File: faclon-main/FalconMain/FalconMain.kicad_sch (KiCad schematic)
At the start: 193 parts, among them J1 Nano-Fit, J2 PTH, J3 Nano-Fit, J4 100mil, J5 Nano-Fit, J6 100mil, J7 Nano-Fit, J8 DNP, J9 JST-XH, Q1 Q_PMOS_GDS, Q10 Q_NMOS_GSD, Q11 Q_PMOS_GSD, Q12 Q_PMOS_GSD, Q13 Q_PMOS_GSD, Q14 Q_PMOS_GSD, Q15 Q_NMOS_GSD, Q16 Q_PMOS_GSD, Q17 Q_PMOS_GSD, Q18 Q_PMOS_GSD, Q19 Q_PMOS_GSD, Q2 Q_PMOS_GDS, Q20 Q_NMOS_GSD, Q21 Q_NMOS_GSD, Q22 Q_PMOS_GDS, Q23 Q_NMOS_GSD, Q24 Q_PMOS_GSD, Q3 Q_NMOS_GDS, Q4 Q_NMOS_GDS, Q5 Q_PMOS_GDS, Q6 Q_PMOS_GDS, Q7 Q_NMOS_GSD, Q8 Q_NMOS_GSD, Q9 Q_NMOS_GSD, U1 MAX1873TEEE+, U2 ADP1883ARMZ-0.6-R7, U3 LTC4412ES6#TRPBF, U4 STM32L152CBT6, U5 BD9E104FJ-E2, U6 AL8843QSP-13, U7 NCP164ASN330T1G, Y1 8MHz, Y2 32.768kHz

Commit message: Design freeze maybe
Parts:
- removed C24, C?: 100uF, Capacitor_THT:CP_Radial_D8.0mm_P3.50mm, symbol Device:C_Polarized_Small
- removed D1, D3, D?: DNP, symbol Device:D_Schottky_Small
- removed Q1, Q5, Q6: Q_PMOS_GDS, symbol Device:Q_PMOS_GDS
- removed R1: 1M, Resistor_SMD:R_0402_1005Metric, symbol Device:R_Small
- removed R18: 0R, Resistor_SMD:R_0402_1005Metric, symbol Device:R_Small
- removed R2: 100k, Resistor_SMD:R_0402_1005Metric, symbol Device:R_Small
- removed R21: 442k, Resistor_SMD:R_0402_1005Metric, symbol Device:R_Small
- removed U3: LTC4412ES6#TRPBF, symbol JetkovKiCADLib:LTC4412ES6#TRPBF
- added C?: 100uF, Capacitor_THT:CP_Radial_D8.0mm_P3.50mm, symbol Device:C_Polarized_Small
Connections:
- net VDC_METERED is gone; now on net VSYS: Q2.3 (S), R13.2, R14.1
- net GND: now also C?.2
- net VSYS: now also C?.1
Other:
- note added: "Charger enabled if DCIN>BATT+220mV Charger disabled if DCIN<BATT+50mV"
- note added: "Design such that diode can replace FET"
- note added: "EXT drives to DCIN-5V"
- note added: "H: VSYS L: VSYS-4.42V"
- note added: "STAT low when SENSE>VIN+20mV Vf of FET Diode < 19.5-17-0.02=2.48V"
- note added: "VDC=VBAT if charger is discconected"
- note added: "Vf(diode)=0.8V"
- note removed: "Can we just use the one ideal diode controller here?"
- note removed: "High: VSYS Low: VSYS-4.42V"
- note removed: "charger"
- moved on the sheet: C1, Q?, R?, U?

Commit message: Finishing up schematics - part footprints
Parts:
- removed Q3, Q4: Q_NMOS_GDS, symbol Device:Q_NMOS_GDS
- added Q2, Q3: Q_NMOS_LFPAK, JetkovKiCADLib:LFPACK56-S08_SOT669_NXP, symbol JetkovKiCADLib:Q_NMOS_LFPAK
- J1, J7: footprint (none) -> JetkovKiCADLib:Molex_Nano-Fit_105309-xx05_1x05_P2.50mm_Vertical
- J2: footprint (none) -> JetkovKiCADLib:Conn_Batt_Wire_10AWG
- J3: footprint (none) -> JetkovKiCADLib:Molex_Nano-Fit_105310-xx12_2x06_P2.50mm_Vertical
- J4: footprint (none) -> Connector_PinHeader_2.54mm:PinHeader_2x03_P2.54mm_Vertical
- J5: footprint (none) -> JetkovKiCADLib:Molex_Nano-Fit_105309-xx02_1x02_P2.50mm_Vertical
- J6: footprint (none) -> Connector_PinHeader_2.54mm:PinHeader_2x15_P2.54mm_Vertical
- J8: footprint (none) -> Connector_PinHeader_2.54mm:PinHeader_1x03_P2.54mm_Vertical
- J9: footprint (none) -> Connector_JST:JST_XH_B5B-XH-AM_1x05_P2.50mm_Vertical
- U2: footprint (none) -> JetkovKiCADLib:10-MSOP_RM-10_AD
- Y1: footprint (none) -> JetkovKiCADLib:Crystal_SMD_HC49_WURTH
- Y2: footprint (none) -> Crystal:Crystal_DS26_D2.0mm_L6.0mm_Horizontal
- gave numbers to parts that had none: 6
- renumbered C20 to C21, C21 to C22, C22 to C23, C23 to C24, D2 to D1, D4 to D2, D5 to D3, D6 to D4, Q2 to Q1, Q11 to Q10, Q12 to Q11, Q13 to Q12, Q14 to Q13, Q15 to Q14, Q16 to Q15, Q17 to Q16, Q18 to Q17, Q19 to Q18, Q20 to Q19, Q21 to Q20, Q22 to Q21, Q23 to Q22, Q24 to Q23, Q7 to Q6, Q8 to Q7, Q9 to Q8, Q10 to Q9, R3 to R1, R12 to R10, R13 to R11, R14 to R12, R15 to R13, R16 to R14, R17 to R15, R19 to R17, R20 to R18, R4 to R2, R22 to R20, R23 to R21, R24 to R22, R25 to R23, R26 to R24, R27 to R25, R28 to R26, R29 to R27, R30 to R28, R31 to R29, R5 to R3, R32 to R30, R33 to R31, R34 to R32, R35 to R33, R36 to R34, R37 to R35, R38 to R36, R39 to R37, R40 to R38, R41 to R39, R6 to R4, R42 to R40, R43 to R41, R44 to R42, R45 to R43, R46 to R44, R47 to R45, R48 to R46, R49 to R47, R50 to R48, R51 to R49, R7 to R5, R52 to R50, R53 to R51, R54 to R52, R55 to R53, R56 to R54, R57 to R55, R58 to R56, R59 to R57, R60 to R58, R61 to R59, R8 to R6, R62 to R60, R63 to R61, R64 to R62, R65 to R63, R66 to R64, R67 to R65, R68 to R66, R69 to R67, R9 to R7, R10 to R8, R11 to R9
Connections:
- net GND: now also Q3.1 (S), Q3.2 (S), Q3.3 (S)
- net VSYS_SW: now also Q2.5 (D)
- net at R15.1: now also Q2.4 (G)
- net at C19.2, L2.1, R18.2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: now also Q2.1 (S), Q2.2 (S), Q2.3 (S), Q3.5 (D)
- net at R17.2, U2.6 (DRVL): now also Q3.4 (G)

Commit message: Add some footprints
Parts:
- removed Q1, Q21, Q4, Q5: Q_PMOS_GDS, symbol Device:Q_PMOS_GDS
- added Q1, Q21, Q4, Q5: Q_PMOS_LFPAK, JetkovKiCADLib:LFPACK56-S08_SOT669_NXP, symbol JetkovKiCADLib:Q_PMOS_LFPAK
- C17, C19, C24, C25, C29, C34, C36, C43, C46, C47, C5: Manufacturer Würth Elektronik -> Murata Electronics; Part Number 885012205061 -> GRM155R71E104KE14D; Voltage 50V -> 25V
- D1, D4: value D_Schottky_Small -> 20A; footprint (none) -> JetkovKiCADLib:TO-252-2-3_DPAK_ST
- D2, D3: footprint (none) -> JetkovKiCADLib:SC-76-SOD-323_USC_TSB
- L1: footprint (none) -> JetkovKiCADLib:DR125-220-R_Handsolder
- L2: footprint (none) -> JetkovKiCADLib:WE-HCI_1365_7443551
- L5: footprint (none) -> JetkovKiCADLib:AMDLA1306S
- Q10, Q11, Q12, Q13, Q15, Q16, Q17, Q18, Q23: footprint (none) -> JetkovKiCADLib:SC-96_TSMT3_ROM
- Q14, Q19, Q20, Q22, Q6, Q7, Q8, Q9: footprint (none) -> JetkovKiCADLib:SOT-323_SC-70
- R14: footprint Resistor_SMD:R_1206_3216Metric -> Resistor_SMD:R_0612_1632Metric; Manufacturer Susumu -> Rohm Semiconductor; Part Number KRL1632E-M-R068-F-T5 -> LTR18EZPFSR068; Power 0.75W -> 1W
- R46, R5: Manufacturer Stackpole Electronics Inc -> Bourns Inc.; Part Number RMCF0402FT133K -> CR0402-FX-1333GLF
- U3: footprint (none) -> JetkovKiCADLib:SOT-23-6_TSOT-23-6_LT
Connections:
- net +19V5: now also Q5.5 (D)
- net VBAT: now also Q4.5 (D)
- net VDC: now also Q4.1 (S), Q4.2 (S), Q4.3 (S), Q5.1 (S), Q5.2 (S), Q5.3 (S)
- net VSYS: now also Q1.1 (S), Q1.2 (S), Q1.3 (S), Q21.1 (S), Q21.2 (S), Q21.3 (S)
- net VSYS_SW: now also Q21.5 (D)
- net at R19.1, U3.4 (STAT): now also Q5.4 (G)
- net at C55.2, Q23.1 (G), R65.2: now also Q21.4 (G)
- net at U1.14 (EXT): now also Q1.4 (G)
- net at D1.1 (K), L1.1: now also Q1.5 (D)
- net at U3.5 (GATE): now also Q4.4 (G)
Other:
- note added: "Could place zener across capacitor to ensure fixed clamp voltage"

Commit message: Reorganize
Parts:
- removed C1, C2: 220nF, Capacitor_SMD:C_0603_1608Metric, symbol Device:C_Small
- removed C10, C16, C18, C22, C3, C45, C50, C51, C52: 10uF, Capacitor_SMD:C_1210_3225Metric, symbol Device:C_Small
- removed C11, C12, C55: 10nF, Capacitor_SMD:C_0402_1005Metric, symbol Device:C_Small
- removed C13, C14: 47nF, Capacitor_SMD:C_0402_1005Metric, symbol Device:C_Small
- removed C15: 1nF, Capacitor_SMD:C_0402_1005Metric, symbol Device:C_Small
- removed C17, C19, C46, C47, C5: 100nF, Capacitor_SMD:C_0402_1005Metric, symbol Device:C_Small
- removed C20, C8: 100uF, Capacitor_THT:CP_Radial_D8.0mm_P3.50mm, symbol Device:C_Polarized_Small
- removed C21: 33uF, Capacitor_THT:CP_Radial_D6.3mm_P2.50mm, symbol Device:C_Polarized_Small
- removed C23: 1.5nF, Capacitor_SMD:C_0402_1005Metric, symbol Device:C_Small
- removed C26, C28, C30, C33: 47uF, Capacitor_SMD:C_1210_3225Metric, symbol Device:C_Small
- removed C35: DNP, Capacitor_THT:CP_Radial_D8.0mm_P3.50mm, symbol Device:C_Polarized_Small
- removed C39, C4, C40, C41, C42, C53, C54, C6: 1uF, Capacitor_SMD:C_0603_1608Metric, symbol Device:C_Small
- removed C48, C9: 510pF, Capacitor_SMD:C_0402_1005Metric, symbol Device:C_Small
- removed C49: 12pF, Capacitor_SMD:C_0402_1005Metric, symbol Device:C_Small
- removed C7: 51pF, Capacitor_SMD:C_0402_1005Metric, symbol Device:C_Small
- removed D1, D4: 20A, JetkovKiCADLib:TO-252-2-3_DPAK_ST, symbol Device:D_Schottky_Small
- removed D2, D3: 500mA, JetkovKiCADLib:SC-76-SOD-323_USC_TSB, symbol Device:D_Schottky_Small
- removed L1: 22uH, JetkovKiCADLib:DR125-220-R_Handsolder, symbol Device:L_Small
- removed L2: 2.0uH, JetkovKiCADLib:WE-HCI_1365_7443551, symbol Device:L_Small
- removed L4: 10uH, Inductor_SMD:L_1008_2520Metric, symbol Device:L_Small
- removed L5: 47uH, JetkovKiCADLib:AMDLA1306S, symbol Device:L_Small
- removed Q1, Q21, Q4, Q5: Q_PMOS_LFPAK, JetkovKiCADLib:LFPACK56-S08_SOT669_NXP, symbol JetkovKiCADLib:Q_PMOS_LFPAK
- removed Q10, Q11, Q12, Q13, Q15, Q16, Q17, Q18, Q23: Q_PMOS_GSD, JetkovKiCADLib:SC-96_TSMT3_ROM, symbol Device:Q_PMOS_GSD
- removed Q14, Q19, Q20, Q22, Q6, Q7, Q8, Q9: Q_NMOS_GSD, JetkovKiCADLib:SOT-323_SC-70, symbol Device:Q_NMOS_GSD
- removed Q2, Q3: Q_NMOS_LFPAK, JetkovKiCADLib:LFPACK56-S08_SOT669_NXP, symbol JetkovKiCADLib:Q_NMOS_LFPAK
- removed R1, R17, R22, R23, R24, R25, R26, R27, R28, R29, R34, R35, R54, R55, R56, R61, R65, R66: 100k, Resistor_SMD:R_0402_1005Metric, symbol Device:R_Small
- removed R10: 10k, Resistor_SMD:R_0402_1005Metric, symbol Device:R_Small
- removed R11: 22m, Resistor_SMD:R_1206_3216Metric, symbol Device:R_Small
- removed R12, R9: 4.7R, Resistor_SMD:R_0402_1005Metric, symbol Device:R_Small
- removed R14: 68m, Resistor_SMD:R_0612_1632Metric, symbol Device:R_Small
- removed R15, R16, R2, R3, R51, R7: 0R, Resistor_SMD:R_0402_1005Metric, symbol Device:R_Small
- removed R18: 2R, Resistor_SMD:R_0402_1005Metric, symbol Device:R_Small
- removed R19, R53: 442k, Resistor_SMD:R_0402_1005Metric, symbol Device:R_Small
- removed R20, R38: 80.6k, Resistor_SMD:R_0402_1005Metric, symbol Device:R_Small
- removed R21: 15k, Resistor_SMD:R_0402_1005Metric, symbol Device:R_Small
- removed R30, R31, R32, R33: 47R, Resistor_SMD:R_2512_6332Metric, symbol Device:R_Small
- removed R36, R4, R52: DNP, Resistor_SMD:R_0402_1005Metric, symbol Device:R_Small
- removed R37, R40, R42, R44, R45, R6, R64: 49.9k, Resistor_SMD:R_0402_1005Metric, symbol Device:R_Small
- removed R39: 221k, Resistor_SMD:R_0402_1005Metric, symbol Device:R_Small
- removed R41: 154k, Resistor_SMD:R_0402_1005Metric, symbol Device:R_Small
- removed R43: 86.6k, Resistor_SMD:R_0402_1005Metric, symbol Device:R_Small
- removed R46, R5: 133k, Resistor_SMD:R_0402_1005Metric, symbol Device:R_Small
- removed R57, R58, R67: 2k, Resistor_SMD:R_0402_1005Metric, symbol Device:R_Small
- removed R59: 44.2k, Resistor_SMD:R_0402_1005Metric, symbol Device:R_Small
- removed R60: 402k, Resistor_SMD:R_0402_1005Metric, symbol Device:R_Small
- removed R62: 1M, Resistor_SMD:R_0402_1005Metric, symbol Device:R_Small
- removed R63: 39m, Resistor_SMD:R_1206_3216Metric, symbol Device:R_Small
- removed R8: 27.4k, Resistor_SMD:R_0402_1005Metric, symbol Device:R_Small
- removed U1: MAX1873TEEE+, JetkovKiCADLib:16-SSOP_16-QSOP_MAX, symbol JetkovKiCADLib:MAX1873TEEE+
- removed U2: ADP1883ARMZ-0.6-R7, JetkovKiCADLib:10-MSOP_RM-10_AD, symbol JetkovKiCADLib:ADP1883ARMZ-0.6-R7
- removed U3: LTC4412ES6#TRPBF, JetkovKiCADLib:SOT-23-6_TSOT-23-6_LT, symbol JetkovKiCADLib:LTC4412ES6#TRPBF
- removed U5: BD9E104FJ-E2, JetkovKiCADLib:8-SOIC_8-SOP-J_ROHM, symbol JetkovKiCADLib:BD9E104FJ-E2
- removed U6: AL8843QSP-13, JetkovKiCADLib:8-SOIC_SO-8EP_DIO, symbol JetkovKiCADLib:AL8843QSP-13
- removed U7: NCP164ASN330T1G, JetkovKiCADLib:SOT-23-5_TSOP−5_ON, symbol JetkovKiCADLib:NCP164ASN330T1G
- renumbered C43 to C1, C32 to C10, C34 to C11, C36 to C12, C27 to C2, C31 to C3, C37 to C4, C38 to C5, C44 to C6, C24 to C7, C25 to C8, C29 to C9, F4 to F1, F5 to F2, F1 to F3, F6 to F4, F7 to F5, F9 to F6, F2 to F7, F3 to F8, F8 to F9, J2 to J1, J9 to J2, J6 to J3, J8 to J5, J5 to J6, J1 to J7, J7 to J8, J3 to J9, L3 to L1, R47 to R1, R48 to R2, R49 to R3, R50 to R4, R13 to R5, U4 to U1
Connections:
- no-connect marks 5 -> 4
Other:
- note removed: "12-14pF"
- note removed: "12-19.5V/0.7A to 4V/0.2A Buck Regulator"
- note removed: "12-19.5V/4.7A to 5.1V/10A Buck Regulator"
- note removed: "170mV dropout @ 3.3V/300mA ±2% Accuracy"
- note removed: "19.5V supply enables power to the MCU. MCU should maintain 4V_EN high"
- note removed: "4.2V"
- note removed: "4A"
- note removed: "4V to 3.3V LDO"
- note removed: "AC/DC Adapter Current Limiting -------------------- I_{IN(MAX)}=0.1V/R_{CSS} =0.1V/22mOhms =4.55A"
- note removed: "AC/DC and Battery Power OR-ing"
- note removed: "Accounting for DC bias: C_{OUT}=47*(1-0.424)*4=108uF"
- note removed: "Alt: C_{OUT}=30uF, R_{4}=64.9kOhms, C_{4}=360pF"
- note removed: "BATTERY BALANCING"
- note removed: "BATTERY CHARGING"
- note removed: "C@5.1V=27uF"
- note removed: "Cell Voltage Cutoff Set -------------------- V_{VADJ}=9.5(V_{CELL})-9(V_{REF}) =9.5(4.1V)-9(4.2V)=1.15V R_{2}=R_{1}[V_{VADJ}/(V_{REF}-V_{VADJ})] =133k*(1.15/(4.2-1.15)~=49.9k V_{VADJ}=1.14587V V_{CELL}=(1.14587V+9(4.2V))/9.5=4.0996V"
- note removed: "Charge Current Sense Output -------------------- V_{Iout}=20(R_{CSB} * I_{chg}) =20(0.068)(2.3)=3.2V C_{load} < 5nF Charge Current Set -------------------- V_{ICH-EN}=I_{CHG} * 1.3146"
- note removed: "Charger enabled if DCIN>BATT+220mV Charger disabled if DCIN<BATT+50mV"
- note removed: "Check MOSFET pins numbers!"
- note removed: "Check Min On-Time Spec -------------------- 250ns<=1.75(V_{OUT}/V_{IN}) 250ns<=1.75(4/19)=368ms"
- note removed: "Could place zener across capacitor to ensure fixed clamp voltage"
- note removed: "Design such that diode can replace FET"
- note removed: "Duty Cycle --------- D_{MIN}=5.1/19=0.268 D_{MAX}=5.1/12=0.425"
- note removed: "EXT drives to DCIN-5V"
- note removed: "Enable 4V_SW with VSYS_SW to power the 5.1V buck regulator LV circuits"
- note removed: "FETs prevent current injection into MCU IO pins when MCU is unpowered"
- note removed: "Front LED Driver"
- note removed: "H: VSYS L: VSYS-4.42V"
- note removed: "HIGH POWER 5.1V REGULATION"
- note removed: "HIGH POWER SWITCH"
- note removed: "Heatsink"
- note removed: "I_{Q}=250uA I_{off}=10uA P_{off}=148uW"
- note removed: "I_{off}=10uA P_{off}=148uW"
- note removed: "I_{off}=?"
- note removed: "I_{out}=0.1V/R_{set} R_{set}=0.1V/2.5A ~=0.039R"
- note removed: "I_{q}=350uA CTRL floating"
- note removed: "Keep divider above (n/4)*200k to reduce effect of R_{ds} and reduce power draw"
- note removed: "LOW POWER 4V AND 3.3V REGULATION"
- note removed: "LV PMOS will turn on after HV, and turn off before HV"
- note removed: "Li-ion 4S Charge Regulator Controller"
- note removed: "Li-ion Cell Balancing FETs"
- note removed: "Li-ion Cell Voltage Sensing"
- note removed: "Loop Compensation ---------------- f_{CROSS}=f_{SW}/12=600e3/12=50kHz f_{ZERO}=f_{CROSS}/4=12.5kHz R_{COMP}=[(f_{CROSS}/(F_{CROSS}+F_{ZERO})][2(pi)(f_{CROSS})(C_{OUT})/((G_{M})(A_{CS}))][V_{OUT}/V_{REF}] =[50e3/(50e3+12.5e3)][(2)(pi)(50e3)(C_{OUT})/((500e-6)(A_{CS})][V_{OUT}/0.8] =[(C_{OUT})(V_{OUT})/(A_{CS})][628318530.718] =[(108e-6)(5.1)/13.4][628318530.718] =25.83kOhms~=26.1kOhms -> 27.4kOhms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"
- note removed: "Loop Compensation ------------------------ R_{4}=[(2pi)(V_{OUT})(f_{CRS})(C_{OUT})]/[(V_{FB})(G_{MP})(G_{MA})] =[(2pi)(V_{OUT})(f_{CRS})(C_{OUT})]/[(0.8V)(7A/V)(82uA/V)] =13682.8948(V_{OUT})(f_{CRS})(C_{OUT}) =13682.8948(4)(40e3)(20e-6) =43.785kOhms~=44.2kOhms C_{4}=1/[(2pi)(R_{4})(f_{CRS}/6)] =1/[(2pi)(44.2e3)(40e3/6)] =540pF~=510pF"
- note removed: "MLCC @19V C=6uF"
- note removed: "MOSFET Channel Conduction Loss --------------------- P_{N1,N2(CL)}=[D(R_{ON-UPPER})+(1-D)R_{ON-LOWER)}]I_{LOAD}^2 =[0.32(5e-3)+(1-0.32)(5e-3)]10^2 =0.16+0.34=0.5W MOSFET Driver Loss --------------------- V_{DR}=V_{DD}-V_{F(RECT)}=4-0.320=3.68V P_{DR(LOSS)}=V_{DR}[(f_{SW})(C_{G-UPPER})(V_{DR})+I_{BIAS}]+V_{DD}[(f_{SW})(C_{G-LOWER})(V_{DD})+I_{BIAS}] =3.68[(600e3)(2.5e-9)(3.68)+2e-3]+4[(600e3)(2.5e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"
- note removed: "MOSFET PSMN4R1-30YLC -------------------- R_{DS(ON)@4V}=5mOhms V_{f(DIODE)@10A}=0.75V Q_{G(TOT)@4V}=10nC C_{G(TOT)@4V}=10nC/4V=2.5nF C_{iss}=1.5nF R_{G}=1.9Ohms"
- note removed: "Make footprint compatible with ETQ-P5M2R0YLC"
- note removed: "Max Charge Current Set -------------------- R_{CSB}=0.2V(V_{ICH-EN}/V_{REF})/I_{CHG} =0.2V(3.3V/4.2V)/2.5A ~=62.6mOhms I_{CHG}=0.2V(3.3V/4.2V)/0.068Ohms=2.311A"
- note removed: "Maximum Inductor Ripple Current -------------------------------- dI_{L}=K_{I}(I_{LOAD}) ~=0.33(10)=3.3A Minimum Inductance -------------------------------- L=[(V_{IN}-V_{OUT})/((dI_{L})(f_{SW}))][V_{OUT}/V_{IN}] =[(16-5.1)/((3.3)(600e3))][5.1/16]=1.755uH Inductor Ripple Current with Selected Inductance -------------------------------- dI_{L}=[(16-5.1)/((2e-6)(600e3))][5.1/16]=2.895A K_{I}=2.895/1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"
- note removed: "Maximum Load Capacitance ----------------- C_{LOAD-MAX}=[(t_{ss})(I_{LIM}-I_{OUTMAX}-I_{RPL}/2)/V_{OUT}]-C_{OUT} =[(1.2e-3)(2.1-0.2-0.526/2)/4]-20e-6 =471uF"
- note removed: "Minimum Inductance -------------------- L>{V_{BATT}[V_{DCIN(MAX)}-V_{BATT}]}/{[V_{DCIN(MAX)}][f_{SW}][I_{CHG}][LIR]} >((14.8V)(19.5V-14.8V))/((19.5V)(300kHz)(2.5A)(0.3)) >15.85uH"
- note removed: "Minimum Input Capacitance -------------------- V_{CIN-MAX-RPL}=0.01(V_{IN-MIN})+([I_{LOAD-MAX})(ESR_{CIN}) =0.01(12)-(10)(0.005)=70mV C_{IN-MIN}=[I_{LOAD-MAX}/V_{MAX-RPL}][D(1-D)/f_{SW}] =[10/0.07][0.425(1-0.425)/600e3]=58.1uF Minimum Output Capacitance ------------------------- dV_{OUTRR}=(0.01)V_{OUT}=(0.005)5.1=0.051V C_{OUT}>dI_{L}/[(8)(f_{SW})(dV_{OUTRR}-(dI_{L})(ESR_{COUT}))] >2.895/[(8)(60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"
- note removed: "Minimum Output Capacitance -------------------- C_{OUT}>4.2(1+16.8/18.5)/[(16.8)(300e3)(62.6e-3)]=25.4uF R_{ESR}<0.0626*12/4.2=179mOhms"
- note removed: "Note: Measured voltage may be 50mV lower than true if measured while a discharge FET is conducting (due to parasitic fuse, etc. resistance)"
- note removed: "ON-BOARD LOAD DRIVERS"
- note removed: "Output Voltage Set ----------- R_{T}=R_{B}(V_{OUT}-0.8V)/0.8V =15e3(5.1-0.8)/0.8 =80.625k~=80.6k"
- note removed: "Output Voltage Set ------------------------ V_{OUT}=0.8[(R_{1}+R_{2})/R_{2}] =0.8*[(402+100)/100]=4.016V"
- note removed: "P=CV^{2}(f_{SW}) =(1.5e-9)(5.1^2)(600e3)=0.023"
- note removed: "Piezo Drivers"
- note removed: "Place as close to MOSFETs as possible"
- note removed: "Place dividers and caps close to MCU pins"
- note removed: "RHS"
- note removed: "R_{TH}=(R_{1}//R_{2}) R_{TH(MAX)}=42.7k"
- note removed: "Ripple Current at Selected Inductance ------------------------ I_{RPL}=(V_{OUT})(V_{IN}-V_{OUT})/[(V_{IN})(f_{OSC})(L)] =(4V)(16V-4V)/[(16V)(570kHz)(10uH)] =0.526A Ripple Voltage at Selected Output Capacitance ------------------------ V_{RPL}=I_{RPL}[R_{ESR}+1/(8(C_{OUT})(f_{OSC}))] =(0.526A)[0.005Ohm+1/(8(20uF)(570kHz))] =8.40mV"
- note removed: "STAT low when SENSE>VIN+20mV Vf of FET Diode < 19.5-17-0.02=2.48V"
- note removed: "T_{RC}=(R1//R2)*C C<(1/42.7k)=23.4uF"
- note removed: "VDC=VBAT if charger is discconected"
- note removed: "V_{DD}>=V_{IN}/8+1.5 =20/8+1.5=4V V_{DD}>=V_{OuT}/4 =5.1/4=1.275V"
- note removed: "V_{TL}=0.8V V_{TH}=2.5V"
- note removed: "Valley Current Limiting -------------- I_{VC-LIM}=1.5V/((A_{CS})(R_{ON})) =1.5/((26.7)(5e-3)) =11.23 I_{LOAD-LIM}=I_{VC-LIM}/(1-K_{I}) =11.23/(1-0.29)=15.8A"
- note removed: "Vf(diode)=0.8V"
- note removed: "[ST: AN2834] C>131nF"
- note removed: "f_{OSC}=570kHz f_{CRS}=40kHz"
- note removed: "t_{ON(MIN)}=500nS"
- note removed: "t_{ON}=[L(0.26)(I_{LED})]/[V_{IN}-V_{LED}-I_{LED}(R_{SET}+R_{L}+R_{SW})] =[47uH(0.26)(3A)]/[14.8V-3V-3A(0.039+0.1+0.2)Ohms] =3.3997uS"

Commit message: Layout WIP
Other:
- note added: "pin number order dont match footprint"
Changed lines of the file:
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@@
     (effects (font (size 2 2)) (justify left bottom))
   )
+  (text "pin number order dont match footprint" (at 31.75 207.01 0)
+    (effects (font (size 3 3) (thickness 0.6) bold) (justify left bottom))
+  )
   (text "Phone" (at 81.28 157.48 0)
     (effects (font (size 1.27 1.27)) (justify left bottom))
@@
       (reference "#PWR0103") (unit 1) (value "+5V1") (footprint "")
     )
-    (path "/104d0e6c-1912-4264-aafc-eb7a241cf8f6/76d0515c-fe87-48ae-bc9d-65edfa56b987"
-      (reference "#PWR0104") (unit 1) (value "VBAT") (footprint "")
+    (path "/104d0e6c-1912-4264-aafc-eb7a241cf8f6/35301d6c-5fa6-471e-b47b-82e28f37f9f3"
+      (reference "#PWR0104") (unit 1) (value "VSYS") (footprint "")
     )
     (path "/104d0e6c-1912-4264-aafc-eb7a241cf8f6/d63c464d-d192-482e-a5a6-2b4a3996e9c3"

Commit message: Layout WIP
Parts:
- removed J9: Nano-Fit, JetkovKiCADLib:Molex_Nano-Fit_105310-xx12_2x06_P2.50mm_Vertical, symbol Connector_Generic:Conn_02x06_Odd_Even
- added J9: Nano-Fit, JetkovKiCADLib:Molex_Nano-Fit_105310-xx12_2x06_P2.50mm_Vertical, symbol Connector_Generic:Conn_02x06_Top_Bottom
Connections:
- net 5V1_PHONE: now also J9.7 (Pin_7)
- net 5V1_REAR: now also J9.1 (Pin_1)
- net ACDC_IN: now also J9.9 (Pin_9)
- net BUTTON: now also J9.6 (Pin_6)
- net GND: now also J9.10 (Pin_10), J9.2 (Pin_2), J9.4 (Pin_4), J9.8 (Pin_8)
- net PWM_LED_REAR1: now also J9.5 (Pin_5)
- net PWM_LED_REAR2: now also J9.11 (Pin_11)
- net VSYS_SW_FUSED: now also J9.3 (Pin_3)
- net at R5.2: now also J9.12 (Pin_12)

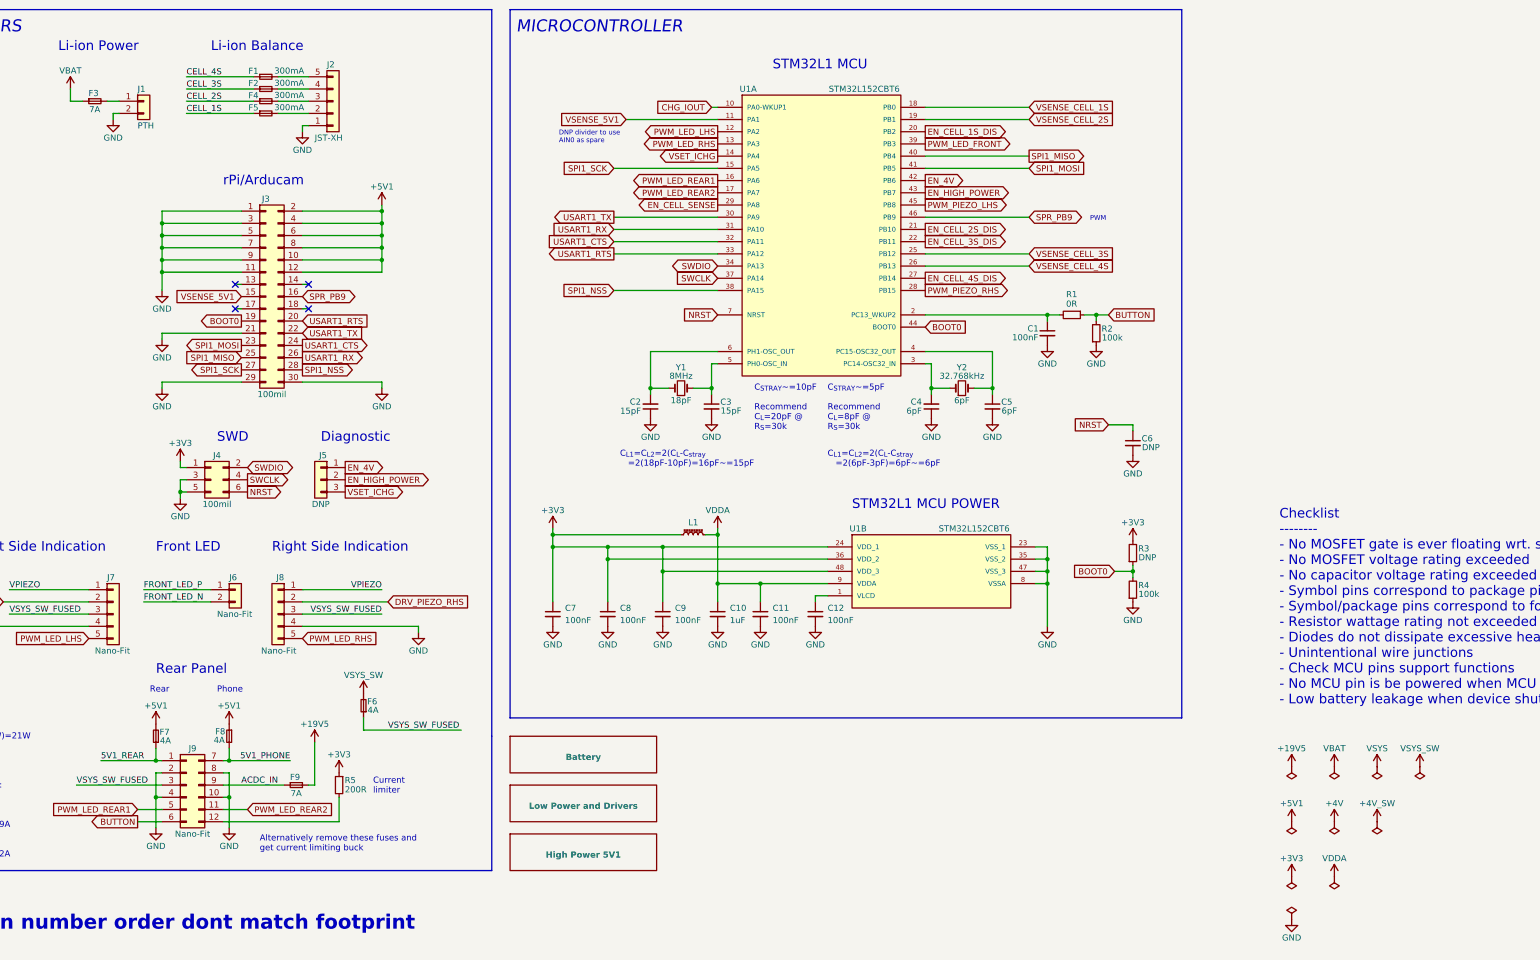
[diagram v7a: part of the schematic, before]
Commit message: Large component rough placement
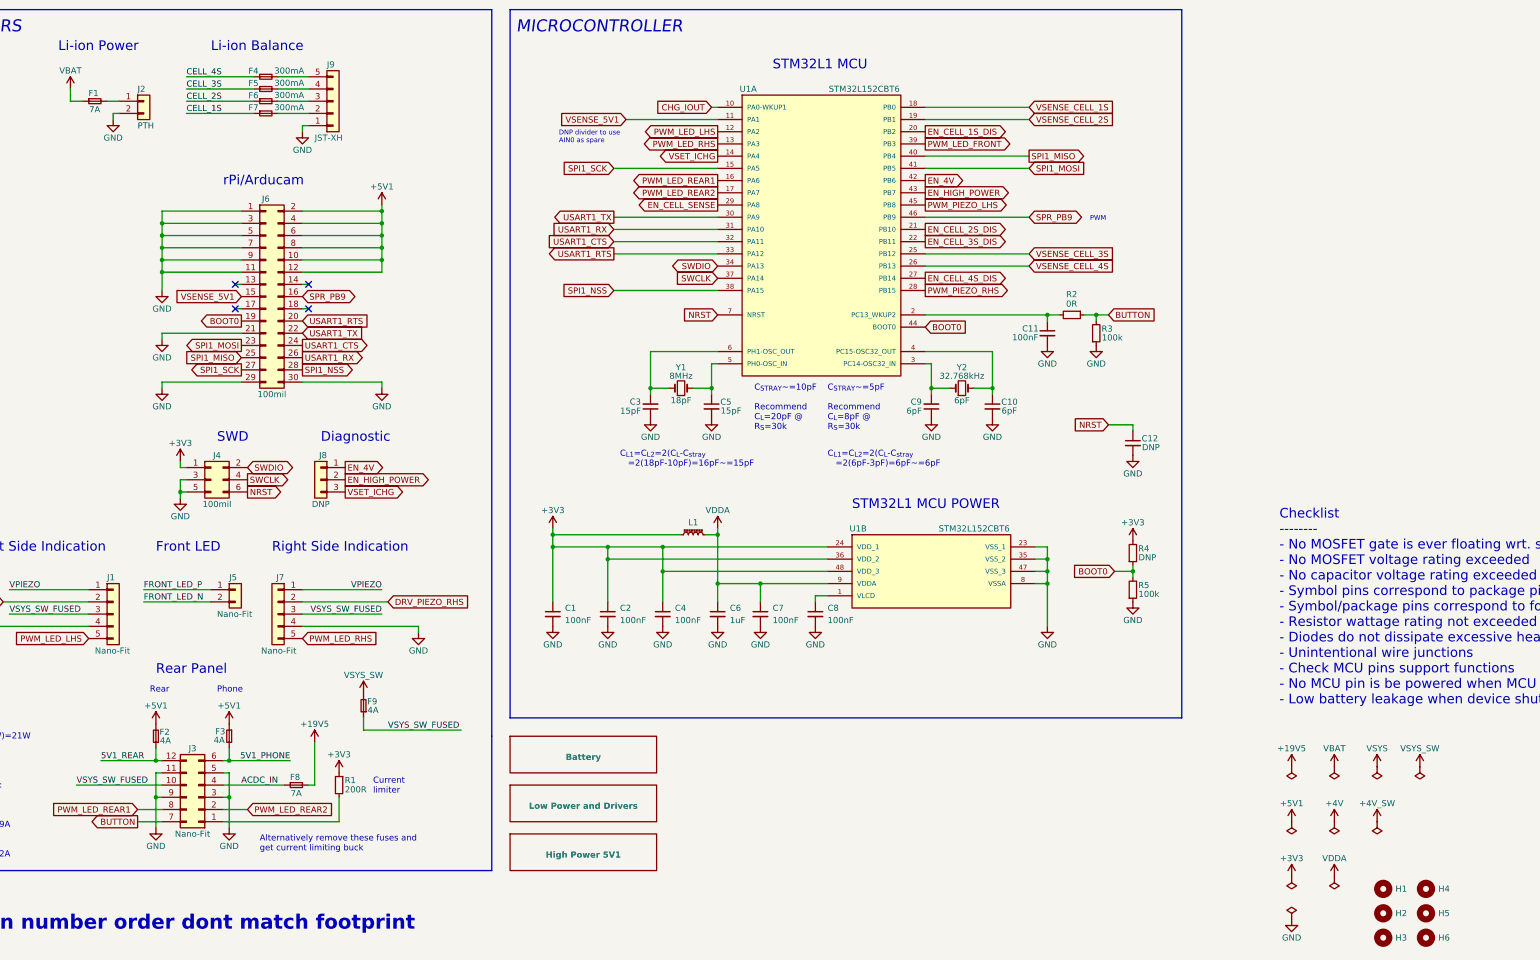
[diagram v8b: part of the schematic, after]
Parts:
- added H1, H2, H3, H4, H5, H6: MountingHole, MountingHole:MountingHole_2.7mm_M2.5, symbol Mechanical:MountingHole
- J9: renamed from J2; footprint Connector_JST:JST_XH_B5B-XH-AM_1x05_P2.50mm_Vertical -> JetkovKiCADLib:JST_XH_B5B-XH-AM_1x05_P2.50mm_Vertical
- Y2: footprint Crystal:Crystal_DS26_D2.0mm_L6.0mm_Horizontal -> JetkovKiCADLib:Crystal_DS26_D2.0mm_L6.0mm_Horizontal
- renumbered C7 to C1, C5 to C10, C1 to C11, C6 to C12, C8 to C2, C2 to C3, C9 to C4, C3 to C5, C10 to C6, C11 to C7, C12 to C8, C4 to C9, F3 to F1, F7 to F2, F8 to F3, F1 to F4, F2 to F5, F4 to F6, F5 to F7, F9 to F8, F6 to F9, J7 to J1, J1 to J2, J9 to J3, J6 to J5, J3 to J6, J8 to J7, J5 to J8, R5 to R1, R1 to R2, R2 to R3, R3 to R4, R4 to R5
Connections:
- net 5V1_PHONE: now also J3.6 (Pin_6); no longer J3.7 (Pin_7)
- net 5V1_REAR: now also J3.12 (Pin_12); no longer J3.1 (Pin_1)
- net ACDC_IN: now also J3.4 (Pin_4); no longer J3.9 (Pin_9)
- net BUTTON: now also J3.7 (Pin_7); no longer J3.6 (Pin_6)
- net GND: now also J3.11 (Pin_11), J3.3 (Pin_3), J3.5 (Pin_5), J3.9 (Pin_9); no longer J3.10 (Pin_10), J3.2 (Pin_2), J3.4 (Pin_4), J3.8 (Pin_8)
- net PWM_LED_REAR1: now also J3.8 (Pin_8); no longer J3.5 (Pin_5)
- net PWM_LED_REAR2: now also J3.2 (Pin_2); no longer J3.11 (Pin_11)
- net VSYS_SW_FUSED: now also J3.10 (Pin_10); no longer J3.3 (Pin_3)
- net at R1.2: now also J3.1 (Pin_1); no longer J3.12 (Pin_12)
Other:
- moved on the sheet: J3
